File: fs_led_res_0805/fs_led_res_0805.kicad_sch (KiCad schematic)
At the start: 4 parts

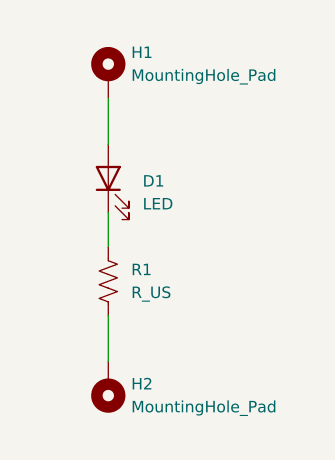
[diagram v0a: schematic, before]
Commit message: update fs_led_res_0805 board revision and export single-unit gerbers
Board/schematic edits since the last panel order. manufacture/jlc/ was
still holding the mismatched resistor_0805_order gerbers (same issue as
fs_led_res_0603); replaced with a fresh export straight from
fs_led_res_0805.kicad_pcb, since this board is now ordered as a single
unit rather than the 1008-up manufacture/led_res_0805_order.kicad_pcb
panel.

Co-Authored-By: Claude Sonnet 5 <noreply@anthropic.com>
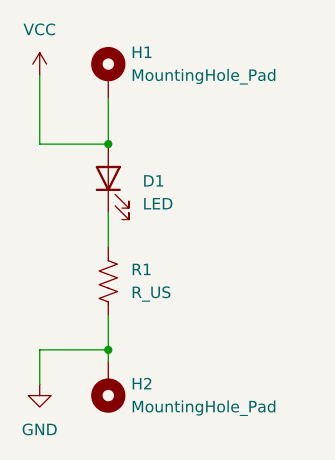
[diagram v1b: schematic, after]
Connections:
- net VCC: now reaches D1.2 (A), H1.1
- net GND: now reaches H2.1, R1.2
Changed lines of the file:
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@@
 		(rev "r1")
 	)
+	(junction
+		(at 113.03 85.09)
+		(diameter 0)
+		(color 0 0 0 0)
+	)
+	(junction
+		(at 113.03 62.23)
+		(diameter 0)
+		(color 0 0 0 0)
+	)
+	(wire
+		(pts
+			(xy 105.41 54.61) (xy 105.41 62.23)
+		)
+		(stroke
+			(width 0)
+			(type default)
+		)
+	)
 	(wire
 		(pts
@@
 	(wire
 		(pts
-			(xy 113.03 81.28) (xy 113.03 86.36)
+			(xy 105.41 85.09) (xy 113.03 85.09)
+		)
+		(stroke
+			(width 0)
+			(type default)
+		)
+	)
+	(wire
+		(pts
+			(xy 105.41 88.9) (xy 105.41 85.09)
+		)
+		(stroke
+			(width 0)
+			(type default)
+		)
+	)
+	(wire
+		(pts
+			(xy 113.03 85.09) (xy 113.03 86.36)
+		)
+		(stroke
+			(width 0)
+			(type default)
+		)
+	)
+	(wire
+		(pts
+			(xy 113.03 81.28) (xy 113.03 85.09)
+		)
+		(stroke
+			(width 0)
+			(type default)
+		)
+	)
+	(wire
+		(pts
+			(xy 105.41 62.23) (xy 113.03 62.23)
 		)
 		(stroke
@@
 			(width 0)
 			(type default)
+		)
+	)
+	(symbol
+		(lib_id "power:VCC")
+		(at 105.41 54.61 0)
+		(unit 1)
+		(body_style 1)
+		(exclude_from_sim no)
+		(in_bom yes)
+		(on_board yes)
+		(in_pos_files yes)
+		(dnp no)
+		(fields_autoplaced yes)
+		(property "Reference" "#PWR01"
+			(at 105.41 58.42 0)
+			(hide yes)
+			(show_name no)
+			(do_not_autoplace no)
+			(effects
+				(font
+					(size 1.27 1.27)
+				)
+			)
+		)
+		(property "Value" "VCC"
+			(at 105.41 49.53 0)
+			(show_name no)
+			(do_not_autoplace no)
+			(effects
+				(font
+					(size 1.27 1.27)
+				)
+			)
+		)
+		(property "Footprint" ""
+			(at 105.41 54.61 0)
+			(hide yes)
+			(show_name no)
+			(do_not_autoplace no)
+			(effects
+				(font
+					(size 1.27 1.27)
+				)
+			)
+		)
+		(property "Datasheet" ""
+			(at 105.41 54.61 0)
+			(hide yes)
+			(show_name no)
+			(do_not_autoplace no)
+			(effects
+				(font
+					(size 1.27 1.27)
+				)
+			)
+		)
+		(property "Description" "Power symbol creates a global label with name \"VCC\""
+			(at 105.41 54.61 0)
+			(hide yes)
+			(show_name no)
+			(do_not_autoplace no)
+			(effects
+				(font
+					(size 1.27 1.27)
+				)
+			)
+		)
+		(pin "1"
+		)
+		(instances
+			(project "fs_led_res_0805"
+				(path "/1bd5fb3b-b787-4e8d-896b-2408c26e0d1d"
+					(reference "#PWR01")
+					(unit 1)
+				)
+			)
 		)
 	)
@@
 					(unit 1)
 				)
+			)
+		)
+	)
+	(symbol
+		(lib_id "power:GND")
+		(at 105.41 88.9 0)
+		(unit 1)
+		(body_style 1)
+		(exclude_from_sim no)
+		(in_bom yes)
+		(on_board yes)
+		(in_pos_files yes)
+		(dnp no)
+		(fields_autoplaced yes)
+		(property "Reference" "#PWR02"
+			(at 105.41 95.25 0)
+			(hide yes)
+			(show_name no)
+			(do_not_autoplace no)
+			(effects
+				(font
+					(size 1.27 1.27)
+				)
+			)
+		)
+		(property "Value" "GND"
+			(at 105.41 93.98 0)
+			(show_name no)
+			(do_not_autoplace no)
+			(effects
+				(font
+					(size 1.27 1.27)
+				)
+			)
+		)
+		(property "Footprint" ""
+			(at 105.41 88.9 0)
+			(hide yes)
+			(show_name no)
+			(do_not_autoplace no)
+			(effects
+				(font
+					(size 1.27 1.27)
+				)
+			)
+		)
+		(property "Datasheet" ""
+			(at 105.41 88.9 0)
+			(hide yes)
+			(show_name no)
+			(do_not_autoplace no)
+			(effects
+				(font
+					(size 1.27 1.27)
+				)
+			)
+		)
+		(property "Description" "Power symbol creates a global label with name \"GND\" , ground"
+			(at 105.41 88.9 0)
+			(hide yes)
+			(show_name no)
+			(do_not_autoplace no)
+			(effects
+				(font
+					(size 1.27 1.27)
+				)
+			)
+		)
+		(pin "1"
+		)
+		(instances
+			(project "fs_led_res_0805"
+				(path "/1bd5fb3b-b787-4e8d-896b-2408c26e0d1d"
+					(reference "#PWR02")
+					(unit 1)
+				)
